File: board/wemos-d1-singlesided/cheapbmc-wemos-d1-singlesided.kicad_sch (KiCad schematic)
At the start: 17 parts, among them J1 Conn_01x02_Male, J3 atxpanel, K1 SILxx-1Axx-71x, K2 SILxx-1Axx-71x, Q1 BC547, Q2 BC547, SW1 SW_Push, U2 FODM217A

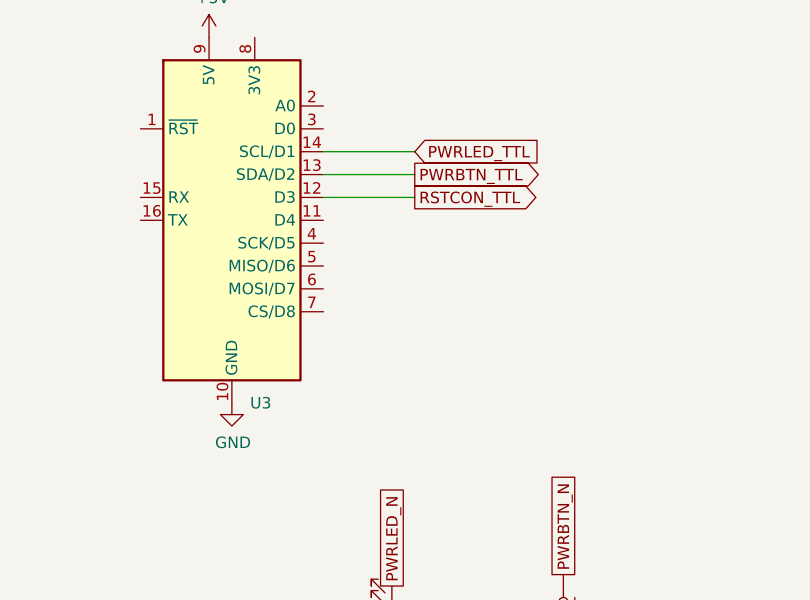
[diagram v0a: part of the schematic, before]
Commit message: wemos: avoid 0.8mm drill because of broken 0.8mm drill bit
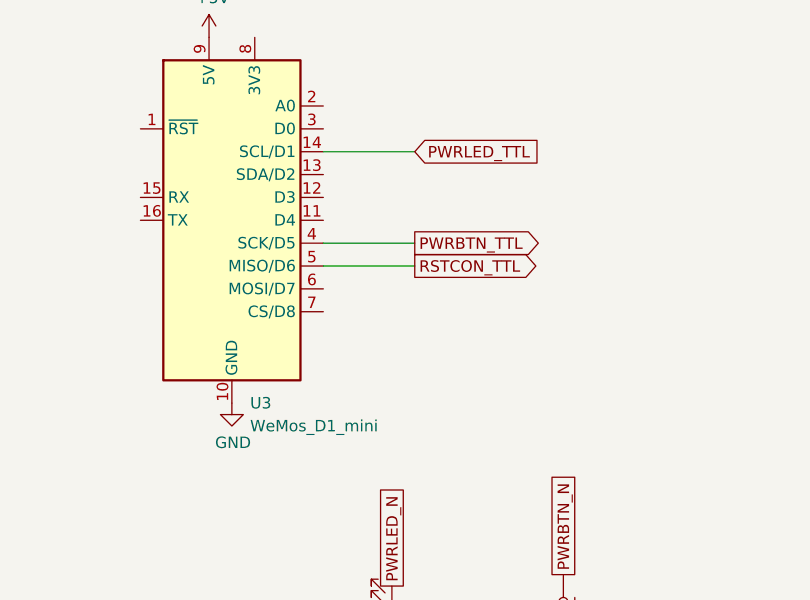
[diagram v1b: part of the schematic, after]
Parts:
- U3: value (none) -> WeMos_D1_mini; footprint (none) -> Module:WEMOS_D1_mini_light
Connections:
- net PWRBTN_TTL: now also U3.4 (SCK/D5); no longer U3.13 (SDA/D2)
- net RSTCON_TTL: now also U3.5 (MISO/D6); no longer U3.12 (D3)
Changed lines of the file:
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@@
     (stroke (width 0) (type default) (color 0 0 0 0))
   )
-  (wire (pts (xy 157.48 66.04) (xy 167.64 66.04))
+  (wire (pts (xy 157.48 73.66) (xy 167.64 73.66))
     (stroke (width 0) (type default) (color 0 0 0 0))
   )
@@
     (stroke (width 0) (type default) (color 0 0 0 0))
   )
-  (wire (pts (xy 157.48 63.5) (xy 167.64 63.5))
+  (wire (pts (xy 157.48 71.12) (xy 167.64 71.12))
     (stroke (width 0) (type default) (color 0 0 0 0))
   )
@@
     )
   )
-  (global_label "PWRBTN_TTL" (shape output) (at 167.64 63.5 0) (fields_autoplaced)
-    (effects (font (size 1.27 1.27)) (justify left))
-    (property "Intersheet References" "${INTERSHEET_REFS}" (id 0) (at -11.43 -6.35 0)
+  (global_label "PWRBTN_TTL" (shape output) (at 167.64 71.12 0) (fields_autoplaced)
+    (effects (font (size 1.27 1.27)) (justify left))
+    (property "Intersheet References" "${INTERSHEET_REFS}" (id 0) (at -11.43 1.27 0)
       (effects (font (size 1.27 1.27)) hide)
     )
@@
     )
   )
-  (global_label "RSTCON_TTL" (shape output) (at 167.64 66.04 0) (fields_autoplaced)
-    (effects (font (size 1.27 1.27)) (justify left))
-    (property "Intersheet References" "${INTERSHEET_REFS}" (id 0) (at -11.43 -6.35 0)
+  (global_label "RSTCON_TTL" (shape output) (at 167.64 73.66 0) (fields_autoplaced)
+    (effects (font (size 1.27 1.27)) (justify left))
+    (property "Intersheet References" "${INTERSHEET_REFS}" (id 0) (at -11.43 1.27 0)
       (effects (font (size 1.27 1.27)) hide)
     )
@@
       (effects (font (size 1.27 1.27)) (justify left))
     )
-    (property "Value" "" (id 1) (at 149.3394 91.44 0)
-      (effects (font (size 1.27 1.27)) (justify left))
-    )
-    (property "Footprint" "" (id 2) (at 147.32 97.79 0)
-      (effects (font (size 1.27 1.27)) hide)
-    )
+    (property "Value" "WeMos_D1_mini" (id 1) (at 149.3394 91.44 0)
+      (effects (font (size 1.27 1.27)) (justify left))
+    )
+    (property "Footprint" "Module:WEMOS_D1_mini_light" (id 2) (at 147.32 97.79 0)
+      (effects (font (size 1.27 1.27)) hide)
+    )
